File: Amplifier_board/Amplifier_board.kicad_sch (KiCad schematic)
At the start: 20 parts, among them U1 TPA3111D1PWPR

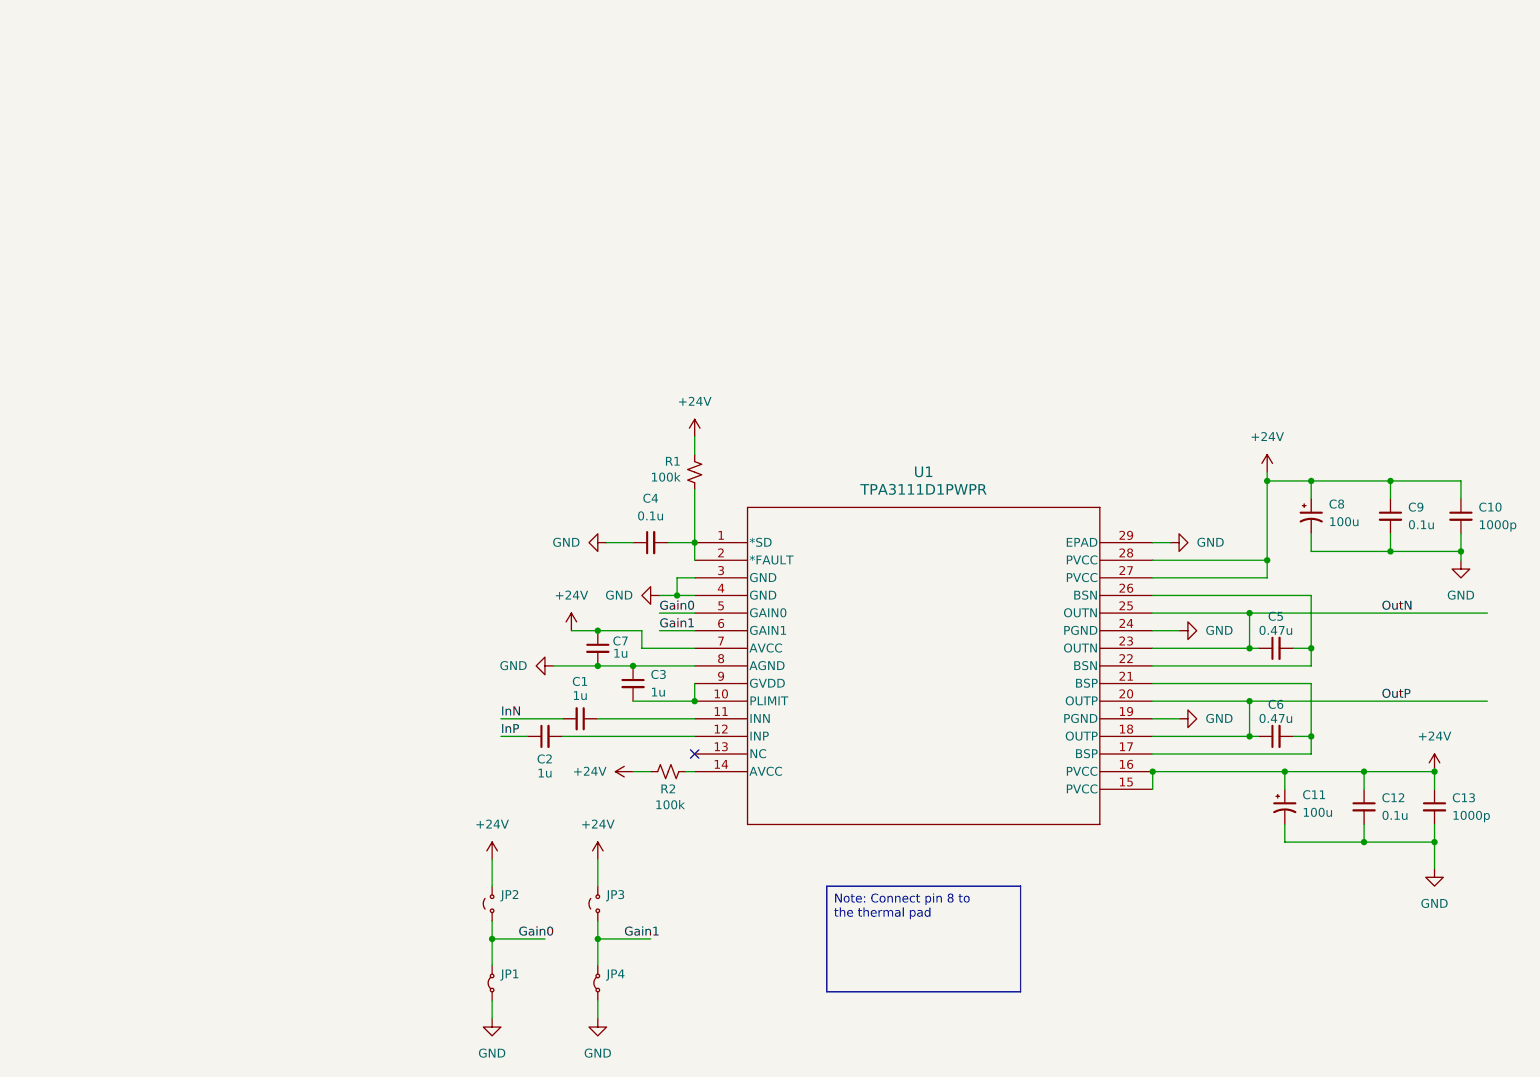
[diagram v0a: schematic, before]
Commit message: Rough draft of amp board schematics
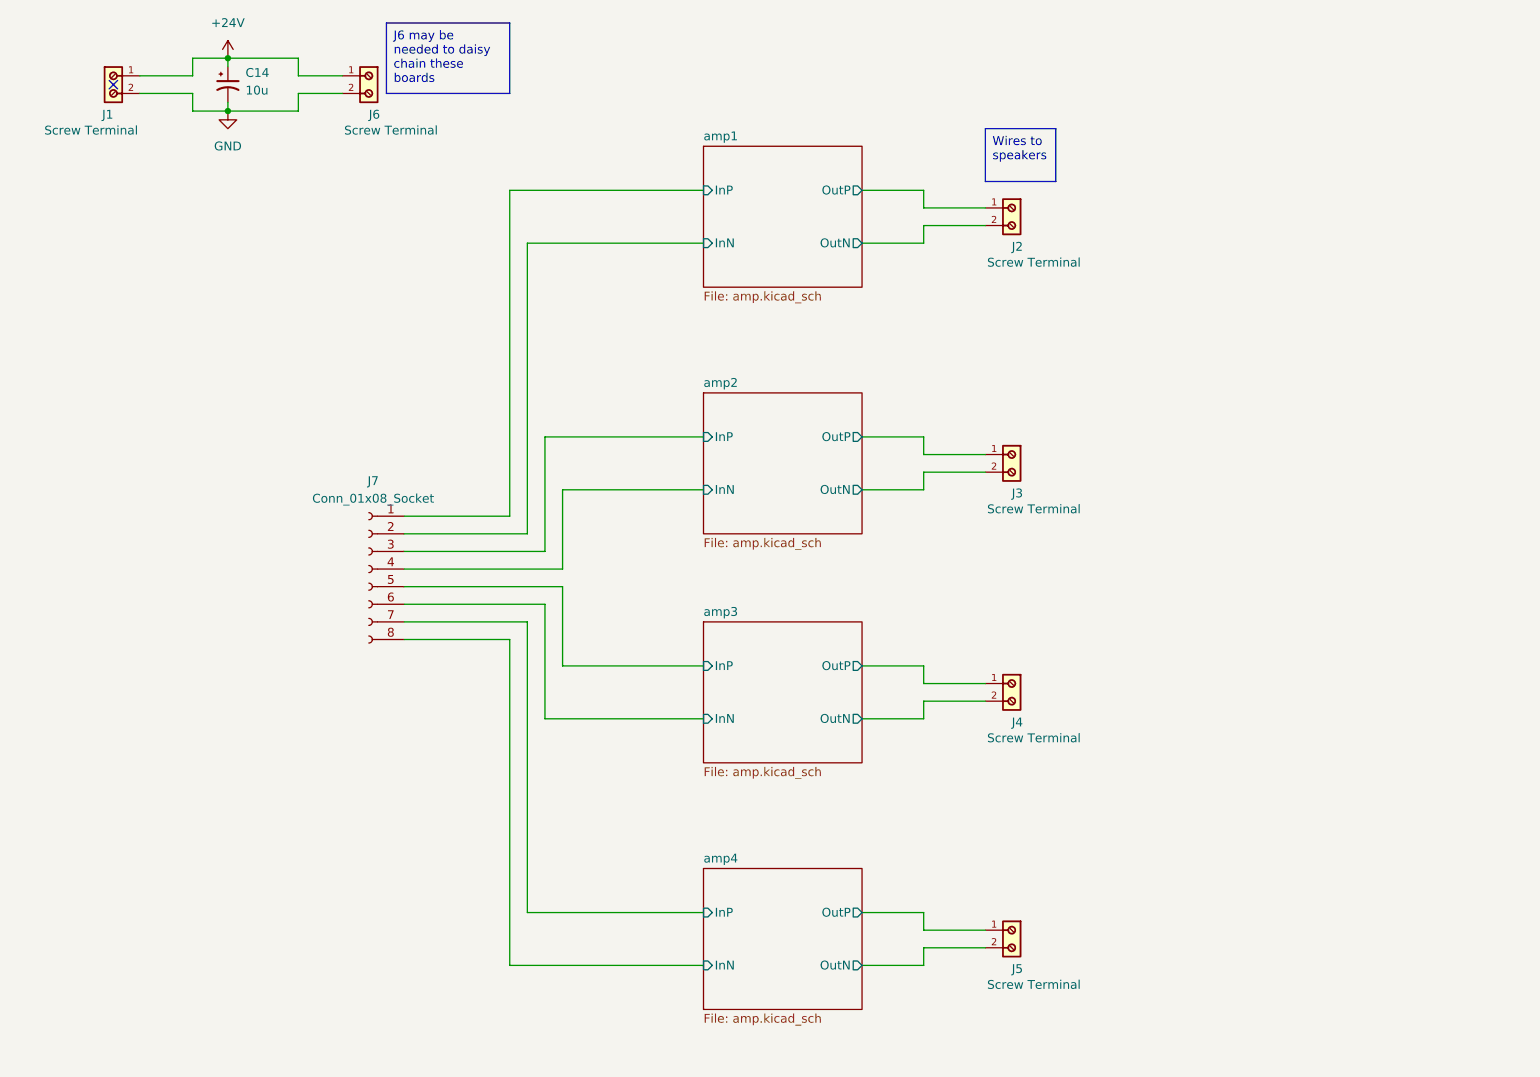
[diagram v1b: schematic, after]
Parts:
- removed C1, C2, C3, C7: 1u, symbol Device:C_Small
- removed C10, C13: 1000p, symbol Device:C_Small
- removed C11, C8: 100u, symbol Device:C_Polarized_Small_US
- removed C12, C4, C9: 0.1u, symbol Device:C_Small
- removed C5, C6: 0.47u, symbol Device:C_Small
- removed JP1, JP4: Jumper_2_Small_Bridged, symbol Jumper:Jumper_2_Small_Bridged
- removed JP2, JP3: Jumper_2_Small_Open, symbol Jumper:Jumper_2_Small_Open
- removed R1, R2: 100k, symbol Device:R_Small_US
- removed U1: TPA3111D1PWPR, PWP28_6P17X2P4, symbol project_lib:TPA3111D1PWPR
- added C14: 10u, symbol Device:C_Polarized_Small_US
- added J1, J2, J3, J4, J5, J6: Screw Terminal, 691137710002:691137710002, symbol project_lib:691137710002
- added J7: Conn_01x08_Socket, symbol Connector:Conn_01x08_Socket
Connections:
- net +24V: now also C14.1, J1.1, J6.1
- net GND: now also C14.2, J1.2, J6.2
- new net amp1/InN: J7.2 (Pin_2)
- new net amp1/InP: J7.1 (Pin_1)
- new net amp1/OutN: J2.2
- new net amp1/OutP: J2.1
- new net amp2/InN: J7.4 (Pin_4)
- new net amp2/InP: J7.3 (Pin_3)
- new net amp2/OutN: J3.2
- new net amp2/OutP: J3.1
- new net amp3/InN: J7.6 (Pin_6)
- new net amp3/InP: J7.5 (Pin_5)
- new net amp3/OutN: J4.2
- new net amp3/OutP: J4.1
- new net amp4/InN: J7.8 (Pin_8)
- new net amp4/InP: J7.7 (Pin_7)
- new net amp4/OutN: J5.2
- new net amp4/OutP: J5.1
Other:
- added sheet amp1 (amp.kicad_sch)
- added sheet amp2 (amp.kicad_sch)
- added sheet amp3 (amp.kicad_sch)
- added sheet amp4 (amp.kicad_sch)

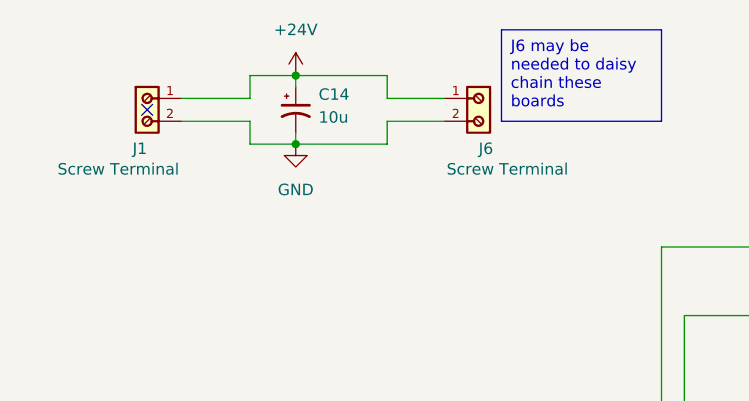
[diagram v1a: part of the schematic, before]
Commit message: Added buffers at DAC outputs
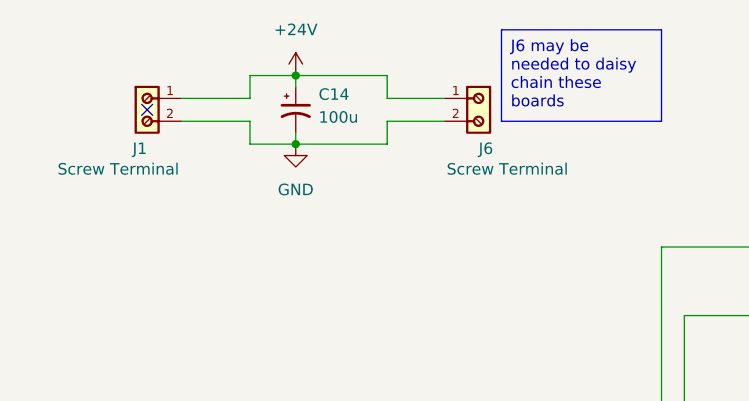
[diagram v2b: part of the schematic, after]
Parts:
- C14: value 10u -> 100u
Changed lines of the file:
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@@
 			)
 		)
-		(property "Value" "10u"
+		(property "Value" "100u"
 			(at 45.72 27.5081 0)
 			(effects

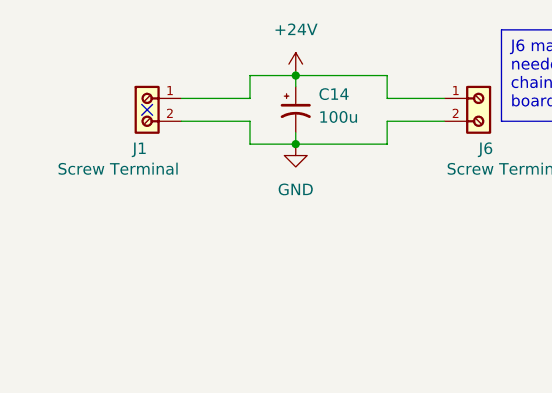
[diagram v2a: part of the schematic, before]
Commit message: Added 2.5V regulator circuit, jumpers on buffers
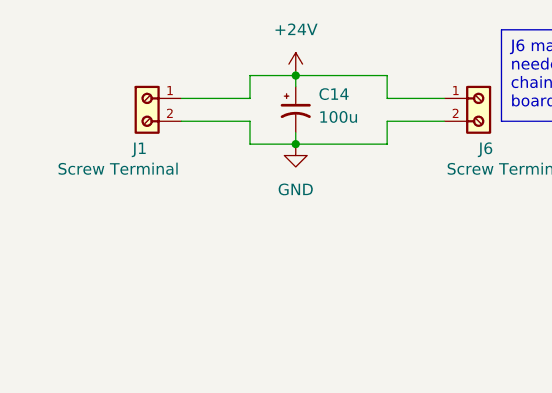
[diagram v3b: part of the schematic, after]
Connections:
- no-connect marks 1 -> 0
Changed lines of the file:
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@@
 		(color 0 0 0 0)
-	)
-	(no_connect
-		(at 26.67 26.67)
 	)
 	(wire

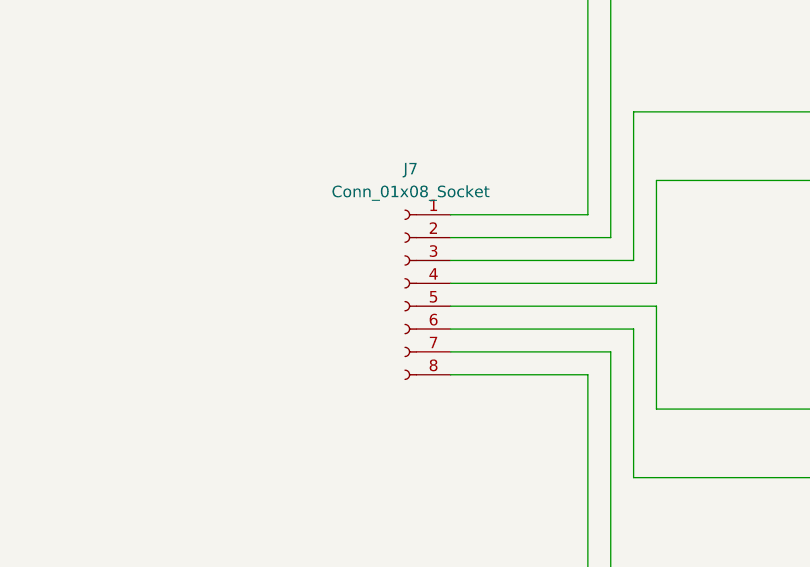
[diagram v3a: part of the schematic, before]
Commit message: Added footprints for amplifier board
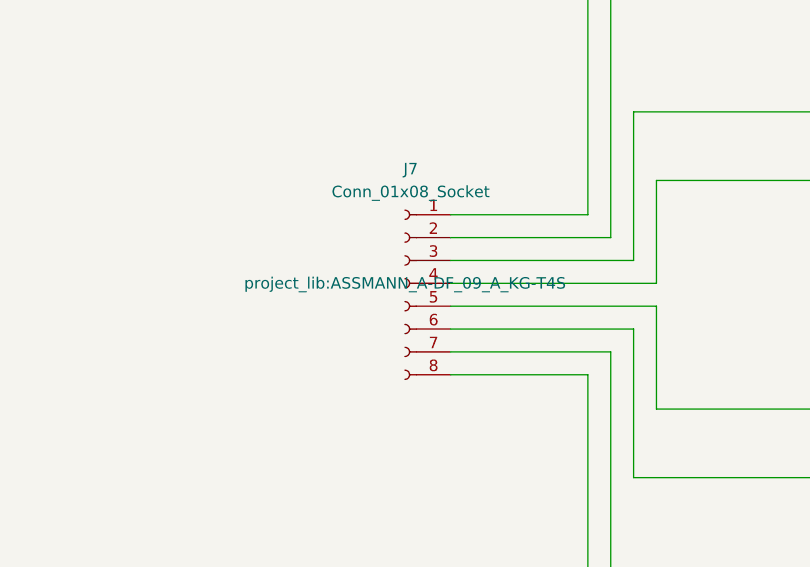
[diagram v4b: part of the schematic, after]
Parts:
- C14: footprint (none) -> Capacitor_SMD:C_0805_2012Metric_Pad1.18x1.45mm_HandSolder
- J7: footprint (none) -> project_lib:ASSMANN_A-DF_09_A_KG-T4S
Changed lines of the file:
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@@
 			)
 		)
-		(property "Footprint" ""
+		(property "Footprint" "Capacitor_SMD:C_0805_2012Metric_Pad1.18x1.45mm_HandSolder"
 			(at 43.18 26.67 0)
 			(effects
@@
 			)
 		)
-		(property "Footprint" ""
+		(property "Footprint" "project_lib:ASSMANN_A-DF_09_A_KG-T4S"
 			(at 63.5 96.52 0)
 			(effects
@@
 					(size 1.27 1.27)
 				)
-				(hide yes)
 			)
 		)

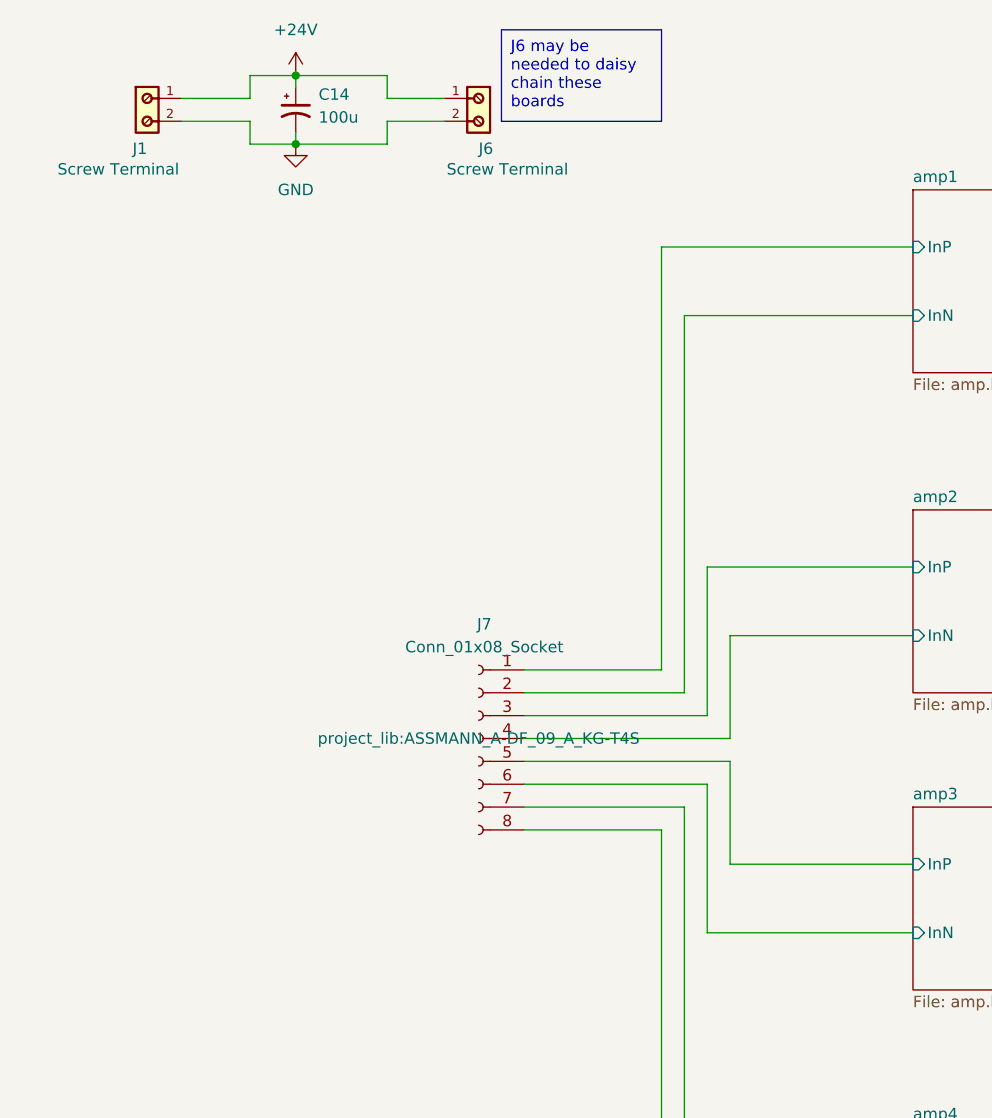
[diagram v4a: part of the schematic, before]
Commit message: Started layout of amplifier board
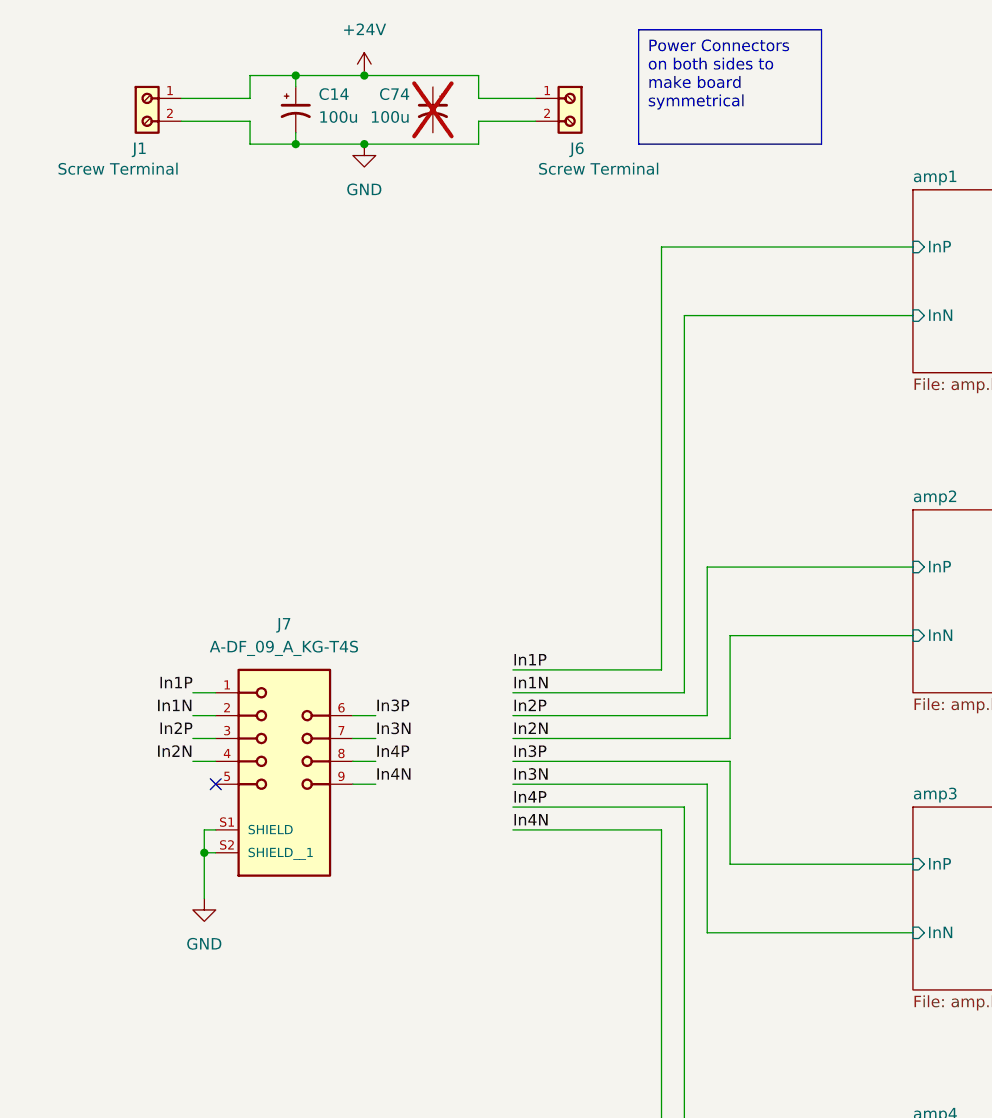
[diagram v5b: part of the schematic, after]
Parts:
- removed J7: Conn_01x08_Socket, project_lib:ASSMANN_A-DF_09_A_KG-T4S, symbol Connector:Conn_01x08_Socket
- added C74: 100u, project_lib:WCAP-ASLI_6.3X7.7_DXL_, symbol Device:C_Polarized_Small_US
- added J7: A-DF_09_A_KG-T4S, project_lib:ASSMANN_A-DF_09_A_KG-T4S, symbol project_lib:A-DF_09_A_KG-T4S
- C14: footprint Capacitor_SMD:C_0805_2012Metric_Pad1.18x1.45mm_HandSolder -> project_lib:WCAP-ASLI_6.3X7.7_DXL_
- J1, J2, J3, J4, J5, J6: footprint 691137710002:691137710002 -> project_lib:691137710002
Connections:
- net GND: now also J7.S1 (SHIELD), J7.S2 (SHIELD__1)
- new net In1N: J7.2
- new net In1P: J7.1
- new net In2N: J7.4
- new net In2P: J7.3
- new net In3N: J7.7
- new net In3P: J7.6
- new net In4N: J7.9
- new net In4P: J7.8
- no-connect marks 0 -> 1
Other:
- moved on the sheet: J6

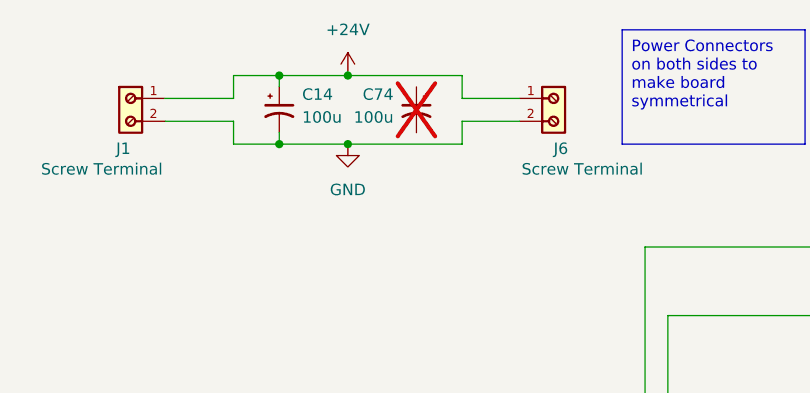
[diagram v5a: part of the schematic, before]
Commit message: Removed buffers on DAC board
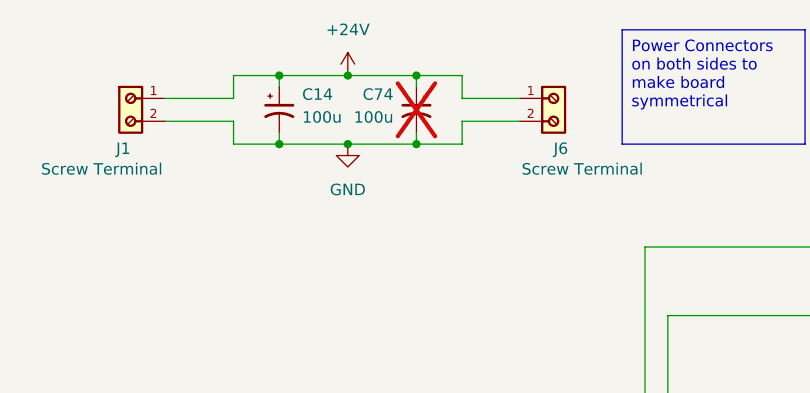
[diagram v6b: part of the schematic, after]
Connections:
- net +24V: now also C74.1
- net GND: now also C74.2
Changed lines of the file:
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@@
 	(paper "A4")
+	(junction
+		(at 58.42 22.86)
+		(diameter 0)
+		(color 0 0 0 0)
+	)
 	(junction
 		(at 43.18 22.86)
@@
 	)
 	(junction
+		(at 58.42 30.48)
+		(diameter 0)
+		(color 0 0 0 0)
+	)
+	(junction
 		(at 50.8 22.86)
 		(diameter 0)
@@
 	(wire
 		(pts
+			(xy 58.42 30.48) (xy 63.5 30.48)
+		)
+		(stroke
+			(width 0)
+			(type default)
+		)
+	)
+	(wire
+		(pts
 			(xy 143.51 49.53) (xy 134.62 49.53)
 		)
@@
 	(wire
 		(pts
+			(xy 58.42 22.86) (xy 63.5 22.86)
+		)
+		(stroke
+			(width 0)
+			(type default)
+		)
+	)
+	(wire
+		(pts
 			(xy 31.75 93.98) (xy 34.29 93.98)
 		)
@@
 	(wire
 		(pts
+			(xy 58.42 22.86) (xy 58.42 24.13)
+		)
+		(stroke
+			(width 0)
+			(type default)
+		)
+	)
+	(wire
+		(pts
 			(xy 31.75 99.06) (xy 34.29 99.06)
 		)
@@
 	(wire
 		(pts
+			(xy 58.42 29.21) (xy 58.42 30.48)
+		)
+		(stroke
+			(width 0)
+			(type default)
+		)
+	)
+	(wire
+		(pts
 			(xy 143.51 146.05) (xy 143.51 148.59)
 		)
@@
 	(wire
 		(pts
-			(xy 50.8 22.86) (xy 63.5 22.86)
+			(xy 50.8 22.86) (xy 58.42 22.86)
 		)
 		(stroke
@@
 	(wire
 		(pts
-			(xy 50.8 30.48) (xy 63.5 30.48)
-		)
-		(stroke
+			(xy 50.8 30.48) (xy 58.42 30.48)
+		)
+		(stroke

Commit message: Added test points, almost finished layout for amp board
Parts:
- added TP33, TP34: 24V, project_lib:TP_RCUCTE, symbol Connector:TestPoint
- added TP35, TP36, TP37, TP38: GND, TestPoint:TestPoint_Bridge_Pitch5.08mm_Drill0.7mm, symbol Connector:TestPoint_2Pole
- C14, C74: footprint project_lib:WCAP-ASLI_6.3X7.7_DXL_ -> Capacitor_THT:CP_Radial_D6.3mm_P2.50mm
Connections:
- net +24V: now also TP33.1, TP34.1
- net GND: now also TP35.1, TP35.2, TP36.1, TP36.2, TP37.1, TP37.2, TP38.1, TP38.2
